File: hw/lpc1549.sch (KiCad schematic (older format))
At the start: 16 parts, among them J301 ARM_JTAG_SWD_HEADER_10_PINSMD, U301 LPC1549JBD64, U302 MCP2551_SOIC8, X301 XTAL_7A-12.000MAAJ-T

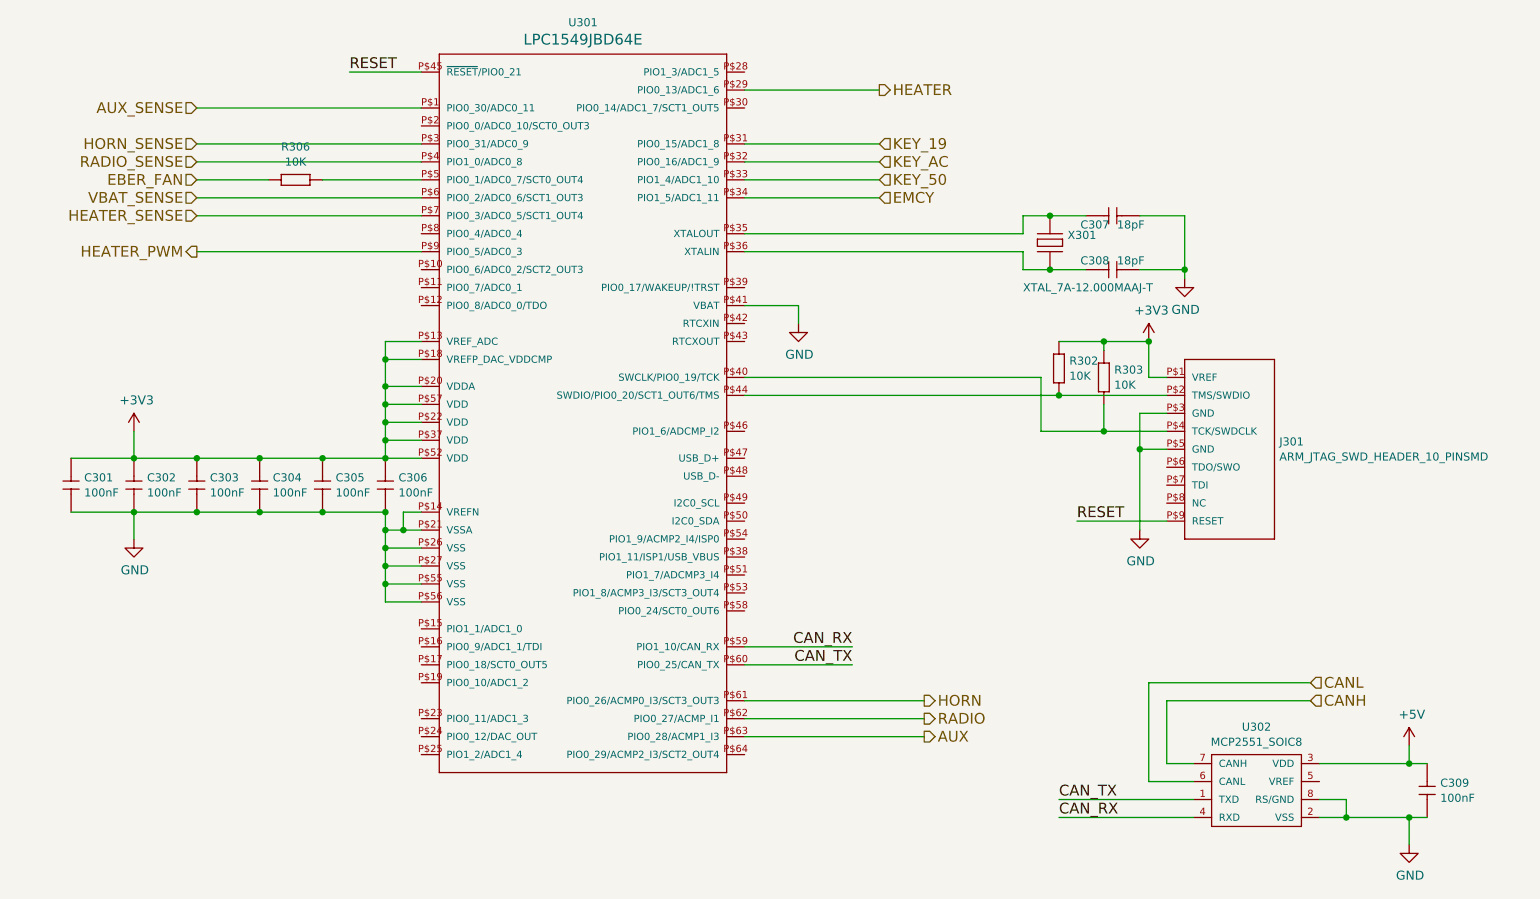
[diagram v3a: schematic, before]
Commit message: heater shuts down when ignition key is turned off
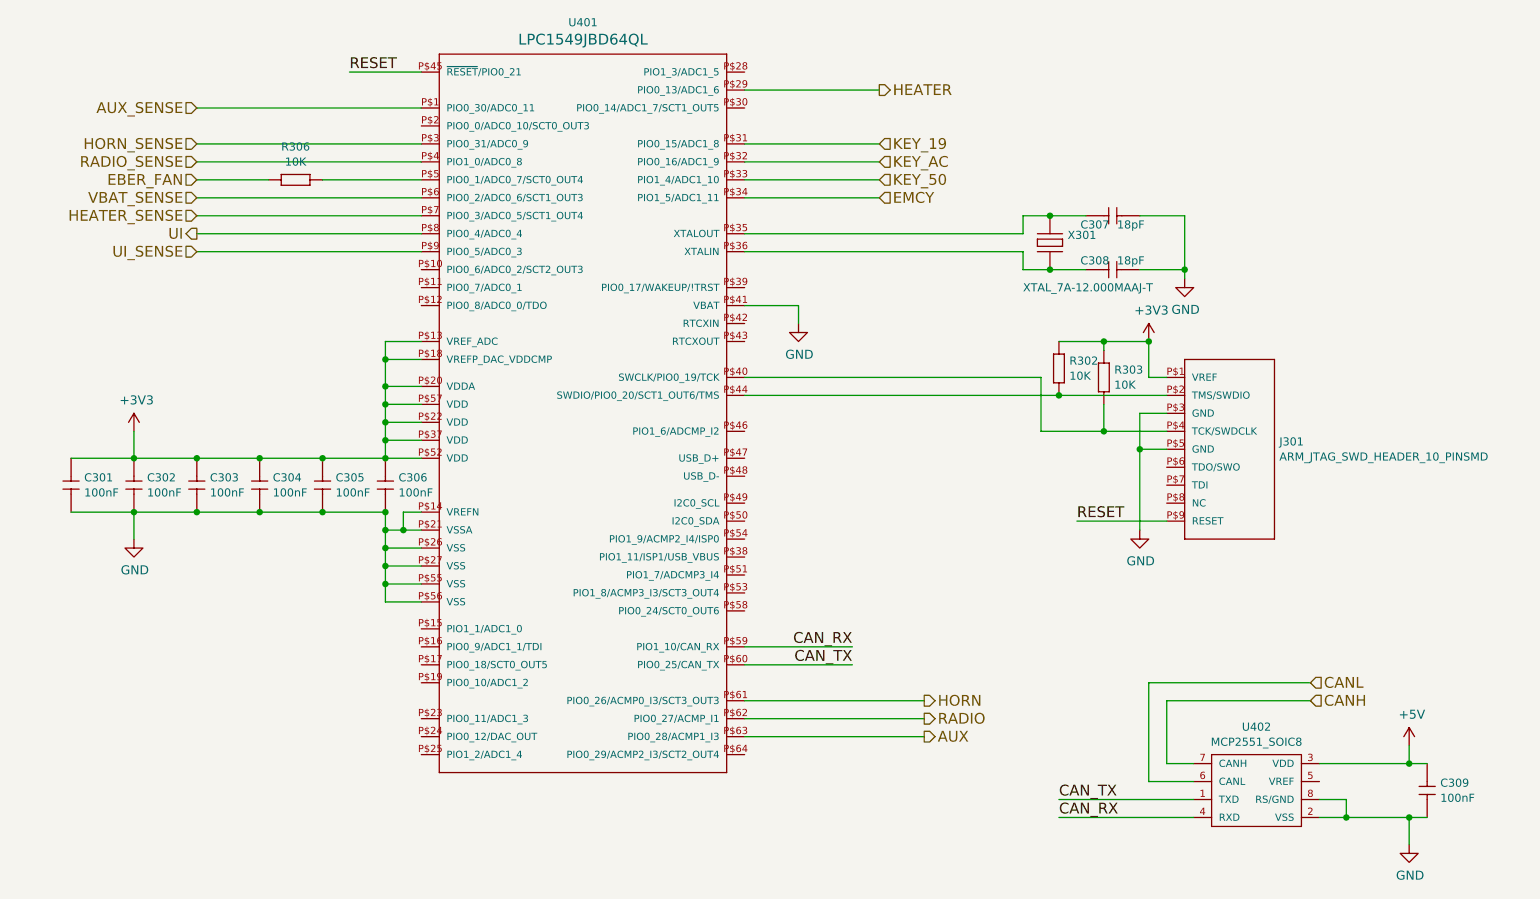
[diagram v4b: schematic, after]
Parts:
- removed U301: LPC1549JBD64, usevolt:QFP64, symbol LPC1549JBD64
- removed U302: MCP2551_SOIC8, usevolt:SOIC8, symbol MCP2551_SOIC8
- added U401: LPC1549JBD64, usevolt:QFP64, symbol LPC1549JBD64
- added U402: MCP2551_SOIC8, usevolt:SOIC8, symbol MCP2551_SOIC8
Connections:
- net +3V3: now also U401.P$13 (VREF_ADC), U401.P$18 (VREFP_DAC_VDDCMP), U401.P$20 (VDDA), U401.P$22 (VDD), U401.P$37 (VDD), U401.P$52 (VDD), U401.P$57 (VDD)
- net +5V: now also U402.3 (VDD)
- net AUX: now also U401.P$63 (PIO0_28/ACMP1_I3)
- net AUX_SENSE: now also U401.P$1 (PIO0_30/ADC0_11)
- net CANH: now also U402.7 (CANH)
- net CANL: now also U402.6 (CANL)
- net CAN_RX: now also U401.P$59 (PIO1_10/CAN_RX), U402.4 (RXD)
- net CAN_TX: now also U401.P$60 (PIO0_25/CAN_TX), U402.1 (TXD)
- net EMCY: now also U401.P$34 (PIO1_5/ADC1_11)
- net GND: now also U401.P$14 (VREFN), U401.P$21 (VSSA), U401.P$26 (VSS), U401.P$27 (VSS), U401.P$41 (VBAT), U401.P$55 (VSS), U401.P$56 (VSS), U402.2 (VSS), U402.8 (RS/GND)
- net HEATER: now also U401.P$29 (PIO0_13/ADC1_6)
- net HEATER_SENSE: now also U401.P$7 (PIO0_3/ADC0_5/SCT1_OUT4)
- net HORN: now also U401.P$61 (PIO0_26/ACMP0_I3/SCT3_OUT3)
- net HORN_SENSE: now also U401.P$3 (PIO0_31/ADC0_9)
- net KEY_19: now also U401.P$31 (PIO0_15/ADC1_8)
- net KEY_50: now also U401.P$33 (PIO1_4/ADC1_10)
- net KEY_AC: now also U401.P$32 (PIO0_16/ADC1_9)
- net RADIO: now also U401.P$62 (PIO0_27/ACMP_I1)
- net RADIO_SENSE: now also U401.P$4 (PIO1_0/ADC0_8)
- net RESET: now also U401.P$45 (~RESET~/PIO0_21)
- net VBAT_SENSE: now also U401.P$6 (PIO0_2/ADC0_6/SCT1_OUT3)
- net at C307.1 (C1), X301.P$1: now also U401.P$35 (XTALOUT)
- net at C308.1 (C1), X301.P$2: now also U401.P$36 (XTALIN)
- net at J301.P$2 (TMS/SWDIO), R302.1 (R1): now also U401.P$44 (SWDIO/PIO0_20/SCT1_OUT6/TMS)
- net at J301.P$4 (TCK/SWDCLK), R303.1 (R1): now also U401.P$40 (SWCLK/PIO0_19/TCK)
- net at R306.1 (R1): now also U401.P$5 (PIO0_1/ADC0_7/SCT0_OUT4)
- new net UI: U401.P$8 (PIO0_4/ADC0_4)
- new net UI_SENSE: U401.P$9 (PIO0_5/ADC0_3)
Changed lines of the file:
@@
 EESchema Schematic File Version 2
+LIBS:fsb-rescue
 LIBS:kemet
 LIBS:power
@@
 $Descr A4 11693 8268
 encoding utf-8
-Sheet 4 9
+Sheet 4 6
 Title ""
 Date ""
@@
 $EndComp
 $Comp
-L +3V3 #PWR018
+L +3V3 #PWR401
 U 1 1 57E689A3
 P 3000 3850
-F 0 "#PWR018" H 3000 3700 50  0001 C CNN
+F 0 "#PWR401" H 3000 3700 50  0001 C CNN
 F 1 "+3V3" H 3015 4023 50  0000 C CNN
 F 2 "" H 3000 3850 50  0000 C CNN
@@
 $EndComp
 $Comp
-L GND #PWR019
+L GND #PWR402
 U 1 1 57E689C9
 P 3000 4450
-F 0 "#PWR019" H 3000 4200 50  0001 C CNN
+F 0 "#PWR402" H 3000 4200 50  0001 C CNN
 F 1 "GND" H 3005 4277 50  0000 C CNN
 F 2 "" H 3000 4450 50  0000 C CNN
@@
 $EndComp
 $Comp
-L GND #PWR020
+L GND #PWR406
 U 1 1 57E697A1
 P 8850 3000
-F 0 "#PWR020" H 8850 2750 50  0001 C CNN
+F 0 "#PWR406" H 8850 2750 50  0001 C CNN
 F 1 "GND" H 8855 2827 50  0000 C CNN
 F 2 "" H 8850 3000 50  0000 C CNN
@@
 $EndComp
 $Comp
-L GND #PWR021
+L GND #PWR403
 U 1 1 57E69A8B
 P 6700 3250
-F 0 "#PWR021" H 6700 3000 50  0001 C CNN
+F 0 "#PWR403" H 6700 3000 50  0001 C CNN
 F 1 "GND" H 6705 3077 50  0000 C CNN
 F 2 "" H 6700 3250 50  0000 C CNN
@@
 $EndComp
 $Comp
-L GND #PWR022
+L GND #PWR404
 U 1 1 5891FBFB
 P 8600 4400
-F 0 "#PWR022" H 8600 4150 50  0001 C CNN
+F 0 "#PWR404" H 8600 4150 50  0001 C CNN
 F 1 "GND" H 8605 4227 50  0000 C CNN
 F 2 "" H 8600 4400 50  0000 C CNN
@@
 $EndComp
 $Comp
-L +3V3 #PWR023
+L +3V3 #PWR405
 U 1 1 5891FCDE
 P 8650 3350
-F 0 "#PWR023" H 8650 3200 50  0001 C CNN
+F 0 "#PWR405" H 8650 3200 50  0001 C CNN
 F 1 "+3V3" H 8665 3523 50  0000 C CNN
 F 2 "" H 8650 3350 50  0000 C CNN
@@
 $EndComp
 $Comp
-L GND #PWR024
+L GND #PWR408
 U 1 1 58C01588
 P 10100 6150
-F 0 "#PWR024" H 10100 5900 50  0001 C CNN
+F 0 "#PWR408" H 10100 5900 50  0001 C CNN
 F 1 "GND" H 10105 5977 50  0000 C CNN
 F 2 "" H 10100 6150 50  0000 C CNN
@@
 $EndComp
 $Comp
-L LPC1549JBD64 U301
-U 1 1 5946DE63
-P 5100 2650
-F 0 "U301" H 5500 3726 45  0000 C CNN
-F 1 "LPC1549JBD64" H 5100 2650 45  0001 L BNN
-F 2 "usevolt:QFP64" H 5130 2800 20  0001 C CNN
-F 3 "http://www.nxp.com/documents/data_sheet/LPC15XX.pdf" H 4710 3570 60  0001 C CNN
-F 4 "2400142" H 5310 4170 60  0001 C CNN "2nd Source Part Number"
-F 5 "Farnell" H 5210 4070 60  0001 C CNN "2nd Source"
-F 6 "568-11350-ND" H 5110 3970 60  0001 C CNN "1st Source Part Number"
-F 7 "Digi-Key" H 5010 3870 60  0001 C CNN "1st Source"
-F 8 "LPC1549JBD64E" H 5500 3631 60  0000 C CNN "Manufacturer Part Number"
-F 9 "NXP" H 4810 3670 60  0001 C CNN "Manufacturer"
-	1    5100 2650
-	1    0    0    -1
-$EndComp
-$Comp
 L ARM_JTAG_SWD_HEADER_10_PINSMD J301
 U 1 1 5953ECE3
@@
 $EndComp
 $Comp
-L MCP2551_SOIC8 U302
-U 1 1 5953EADD
-P 9300 5800
-F 0 "U302" H 9350 6104 45  0000 C CNN
-F 1 "MCP2551_SOIC8" H 9350 6020 45  0000 C CNN
-F 2 "usevolt:SOIC8" H 9180 5950 20  0001 C CNN
-F 3 "http://www.microchip.com/mymicrochip/filehandler.aspx?ddocname=en011797" H 8900 6250 60  0001 C CNN
-F 4 "9758569" H 9900 6620 60  0001 C CNN "2nd Source Part Number"
-F 5 "Digi-Key" H 9600 6320 60  0001 C CNN "1st Source"
-F 6 "Farnell" H 9800 6520 60  0001 C CNN "2nd Source"
-F 7 "MCP2551-I/SN" H 9500 6220 60  0001 C CNN "Manufacturer Part Number"
-F 8 "MCP2551-I/SN-ND" H 9700 6420 60  0001 C CNN "1st Source Part Number"
-F 9 "MICROCHIP" H 9450 6100 60  0001 C CNN "Manufacturer"
-	1    9300 5800
-	-1   0    0    -1
-$EndComp
-$Comp
-L +5V #PWR025
+L +5V #PWR407
 U 1 1 595E0BE4
 P 10100 5600
-F 0 "#PWR025" H 10100 5450 50  0001 C CNN
+F 0 "#PWR407" H 10100 5450 50  0001 C CNN
 F 1 "+5V" H 10115 5773 50  0000 C CNN
 F 2 "" H 10100 5600 50  0000 C CNN
@@
 Text HLabel 7150 1950 2    60   Output ~ 0
 HEATER
-Text HLabel 3350 2850 0    60   Output ~ 0
-HEATER_PWM
 Text HLabel 7150 2250 2    60   Input ~ 0
 KEY_19
@@
 	6400 1950 7150 1950
 Wire Wire Line
-	3350 2850 4600 2850
-Wire Wire Line
 	6400 2350 7150 2350
 Wire Wire Line
@@
 Wire Wire Line
 	8050 3550 6400 3550
+$Comp
+L LPC1549JBD64 U401
+U 1 1 5A05FDBB
+P 5100 2650
+F 0 "U401" H 5500 3726 45  0000 C CNN
+F 1 "LPC1549JBD64" H 5100 2650 45  0001 L BNN
+F 2 "usevolt:QFP64" H 5130 2800 20  0001 C CNN
+F 3 "http://www.nxp.com/documents/data_sheet/LPC15XX.pdf" H 4710 3570 60  0001 C CNN
+F 4 "2400142" H 5310 4170 60  0001 C CNN "2nd Source Part Number"
+F 5 "Farnell" H 5210 4070 60  0001 C CNN "2nd Source"
+F 6 "568-11350-ND" H 5110 3970 60  0001 C CNN "1st Source Part Number"
+F 7 "Digi-Key" H 5010 3870 60  0001 C CNN "1st Source"
+F 8 "LPC1549JBD64QL" H 5500 3631 60  0000 C CNN "Manufacturer Part Number"
+F 9 "NXP" H 4810 3670 60  0001 C CNN "Manufacturer"
+	1    5100 2650
+	1    0    0    -1
+$EndComp
+$Comp
+L MCP2551_SOIC8 U402
+U 1 1 5A060268
+P 9300 5800
+F 0 "U402" H 9350 6104 45  0000 C CNN
+F 1 "MCP2551_SOIC8" H 9350 6020 45  0000 C CNN
+F 2 "usevolt:SOIC8" H 9180 5950 20  0001 C CNN
+F 3 "http://www.microchip.com/mymicrochip/filehandler.aspx?ddocname=en011797" H 8900 6250 60  0001 C CNN
+F 4 "9758569" H 9900 6620 60  0001 C CNN "2nd Source Part Number"
+F 5 "Digi-Key" H 9600 6320 60  0001 C CNN "1st Source"
+F 6 "Farnell" H 9800 6520 60  0001 C CNN "2nd Source"
+F 7 "MCP2551-I/SN" H 9500 6220 60  0001 C CNN "Manufacturer Part Number"
+F 8 "MCP2551-I/SN-ND" H 9700 6420 60  0001 C CNN "1st Source Part Number"
+F 9 "MICROCHIP" H 9450 6100 60  0001 C CNN "Manufacturer"
+	1    9300 5800
+	-1   0    0    -1
+$EndComp
+Wire Wire Line
+	4600 2750 3350 2750
+Wire Wire Line
+	4600 2850 3350 2850
+Text HLabel 3350 2750 0    60   Output ~ 0
+UI
+Text HLabel 3350 2850 0    60   Input ~ 0
+UI_SENSE
 $EndSCHEMATC

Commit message: hw 2.1.0 created, not yet ordered
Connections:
- net AUX: now also U401.P$17 (PIO0_18/SCT0_OUT5); no longer U401.P$63 (PIO0_28/ACMP1_I3)
- net AUX_SENSE: now also U401.P$19 (PIO0_10/ADC1_2); no longer U401.P$1 (PIO0_30/ADC0_11)
- net EMCY: now also U401.P$32 (PIO0_16/ADC1_9); no longer U401.P$34 (PIO1_5/ADC1_11)
- net HEATER: now also U401.P$28 (PIO1_3/ADC1_5); no longer U401.P$29 (PIO0_13/ADC1_6)
- net HEATER_SENSE: now also U401.P$25 (PIO1_2/ADC1_4); no longer U401.P$7 (PIO0_3/ADC0_5/SCT1_OUT4)
- net HORN: now also U401.P$8 (PIO0_4/ADC0_4); no longer U401.P$61 (PIO0_26/ACMP0_I3/SCT3_OUT3)
- net HORN_SENSE: now also U401.P$9 (PIO0_5/ADC0_3); no longer U401.P$3 (PIO0_31/ADC0_9)
- net KEY_19: now also U401.P$30 (PIO0_14/ADC1_7/SCT1_OUT5); no longer U401.P$31 (PIO0_15/ADC1_8)
- net KEY_50: now also U401.P$29 (PIO0_13/ADC1_6); no longer U401.P$33 (PIO1_4/ADC1_10)
- net KEY_AC: now also U401.P$31 (PIO0_15/ADC1_8); no longer U401.P$32 (PIO0_16/ADC1_9)
- net RADIO: now also U401.P$7 (PIO0_3/ADC0_5/SCT1_OUT4); no longer U401.P$62 (PIO0_27/ACMP_I1)
- net RADIO_SENSE: now also U401.P$10 (PIO0_6/ADC0_2/SCT2_OUT3); no longer U401.P$4 (PIO1_0/ADC0_8)
- net UI: now also U401.P$11 (PIO0_7/ADC0_1); no longer U401.P$8 (PIO0_4/ADC0_4)
- net UI_SENSE: now also U401.P$12 (PIO0_8/ADC0_0/TDO); no longer U401.P$9 (PIO0_5/ADC0_3)
- new net DOORSW1: U401.P$33 (PIO1_4/ADC1_10)
- new net DOORSW2: U401.P$34 (PIO1_5/ADC1_11)
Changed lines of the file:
@@
 Text HLabel 3350 2450 0    60   Input ~ 0
 EBER_FAN
-Text HLabel 7400 5350 2    60   Output ~ 0
+Text HLabel 3350 2750 0    60   Output ~ 0
 HORN
-Text HLabel 3350 2250 0    60   Input ~ 0
+Text HLabel 3350 2850 0    60   Input ~ 0
 HORN_SENSE
-Text HLabel 7400 5450 2    60   Output ~ 0
+Text HLabel 3350 2650 0    60   Output ~ 0
 RADIO
-Text HLabel 3350 2350 0    60   Input ~ 0
+Text HLabel 3350 2950 0    60   Input ~ 0
 RADIO_SENSE
-Text HLabel 3350 2050 0    60   Input ~ 0
+Text HLabel 3350 5250 0    60   Input ~ 0
 AUX_SENSE
-Text HLabel 7400 5550 2    60   Output ~ 0
+Text HLabel 3350 5150 0    60   Output ~ 0
 AUX
-Text HLabel 7150 1950 2    60   Output ~ 0
+Text HLabel 7150 1850 2    60   Output ~ 0
 HEATER
+Text HLabel 7150 2050 2    60   Input ~ 0
+KEY_19
+Text HLabel 7150 1950 2    60   Input ~ 0
+KEY_50
 Text HLabel 7150 2250 2    60   Input ~ 0
-KEY_19
-Text HLabel 7150 2450 2    60   Input ~ 0
-KEY_50
+KEY_AC
 Text HLabel 7150 2350 2    60   Input ~ 0
-KEY_AC
-Text HLabel 7150 2550 2    60   Input ~ 0
 EMCY
-Text HLabel 3350 2650 0    60   Input ~ 0
+Text HLabel 3350 5650 0    60   Input ~ 0
 HEATER_SENSE
 $Comp
@@
 	3750 2450 3350 2450
 Wire Wire Line
-	6400 5350 7400 5350
-Wire Wire Line
-	4600 2250 3350 2250
-Wire Wire Line
-	6400 5450 7400 5450
-Wire Wire Line
-	4600 2350 3350 2350
-Wire Wire Line
-	4600 2050 3350 2050
-Wire Wire Line
-	6400 5550 7400 5550
+	4600 2750 3350 2750
+Wire Wire Line
+	4600 2850 3350 2850
+Wire Wire Line
+	4600 2650 3350 2650
+Wire Wire Line
+	4600 2950 3350 2950
+Wire Wire Line
+	4600 5250 3350 5250
+Wire Wire Line
+	4600 5150 3350 5150
+Wire Wire Line
+	6400 1850 7150 1850
+Wire Wire Line
+	6400 2250 7150 2250
 Wire Wire Line
 	6400 1950 7150 1950
 Wire Wire Line
+	6400 2050 7150 2050
+Wire Wire Line
 	6400 2350 7150 2350
 Wire Wire Line
-	6400 2450 7150 2450
-Wire Wire Line
-	6400 2250 7150 2250
-Wire Wire Line
-	6400 2550 7150 2550
-Wire Wire Line
-	4600 2650 3350 2650
+	4600 5650 3350 5650
 Wire Wire Line
 	4600 2550 3350 2550
@@
 $EndComp
 Wire Wire Line
-	4600 2750 3350 2750
-Wire Wire Line
-	4600 2850 3350 2850
-Text HLabel 3350 2750 0    60   Output ~ 0
+	4600 3050 3350 3050
+Wire Wire Line
+	4600 3150 3350 3150
+Text HLabel 3350 3050 0    60   Output ~ 0
 UI
-Text HLabel 3350 2850 0    60   Input ~ 0
+Text HLabel 3350 3150 0    60   Input ~ 0
 UI_SENSE
+Wire Wire Line
+	6400 2450 6800 2450
+Wire Wire Line
+	6400 2550 6800 2550
+Text HLabel 6800 2450 2    60   Input ~ 0
+DOORSW1
+Text HLabel 6800 2550 2    60   Input ~ 0
+DOORSW2
 $EndSCHEMATC

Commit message: making 2.2.0 pcb
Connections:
- net DOORSW1: now also U401.P$54 (PIO1_9/ACMP2_I4/ISP0); no longer U401.P$33 (PIO1_4/ADC1_10)
- net DOORSW2: now also U401.P$33 (PIO1_4/ADC1_10); no longer U401.P$34 (PIO1_5/ADC1_11)
- new net SEATSW: U401.P$34 (PIO1_5/ADC1_11)
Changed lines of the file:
@@
 $Descr A4 11693 8268
 encoding utf-8
-Sheet 4 6
+Sheet 4 8
 Title ""
 Date ""
@@
 Wire Wire Line
 	6400 2550 6800 2550
+Text HLabel 6800 4450 2    60   Input ~ 0
+DOORSW1
 Text HLabel 6800 2450 2    60   Input ~ 0
-DOORSW1
+DOORSW2
+Wire Wire Line
+	6400 4450 6800 4450
 Text HLabel 6800 2550 2    60   Input ~ 0
-DOORSW2
+SEATSW
 $EndSCHEMATC
